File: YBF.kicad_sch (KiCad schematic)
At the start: 17 parts, among them J1 Chain_LED_out, J2 Chain_LED_return, SW1 1825910-6, SW2 1825910-6

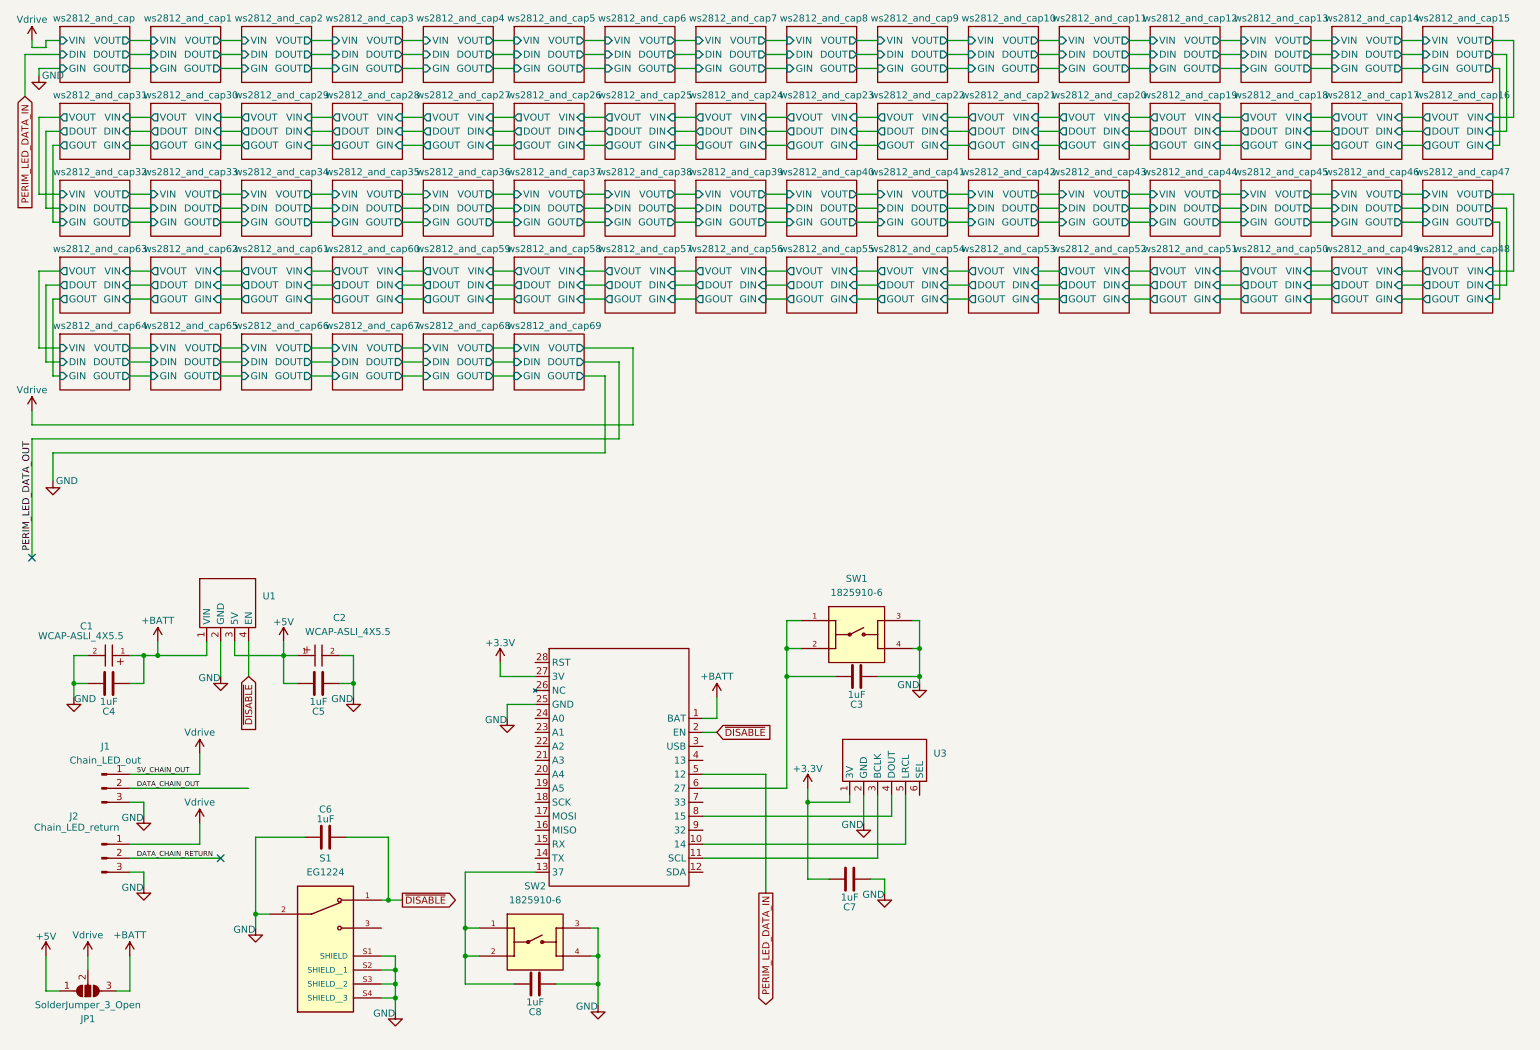
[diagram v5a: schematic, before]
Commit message: Add chain loop holes
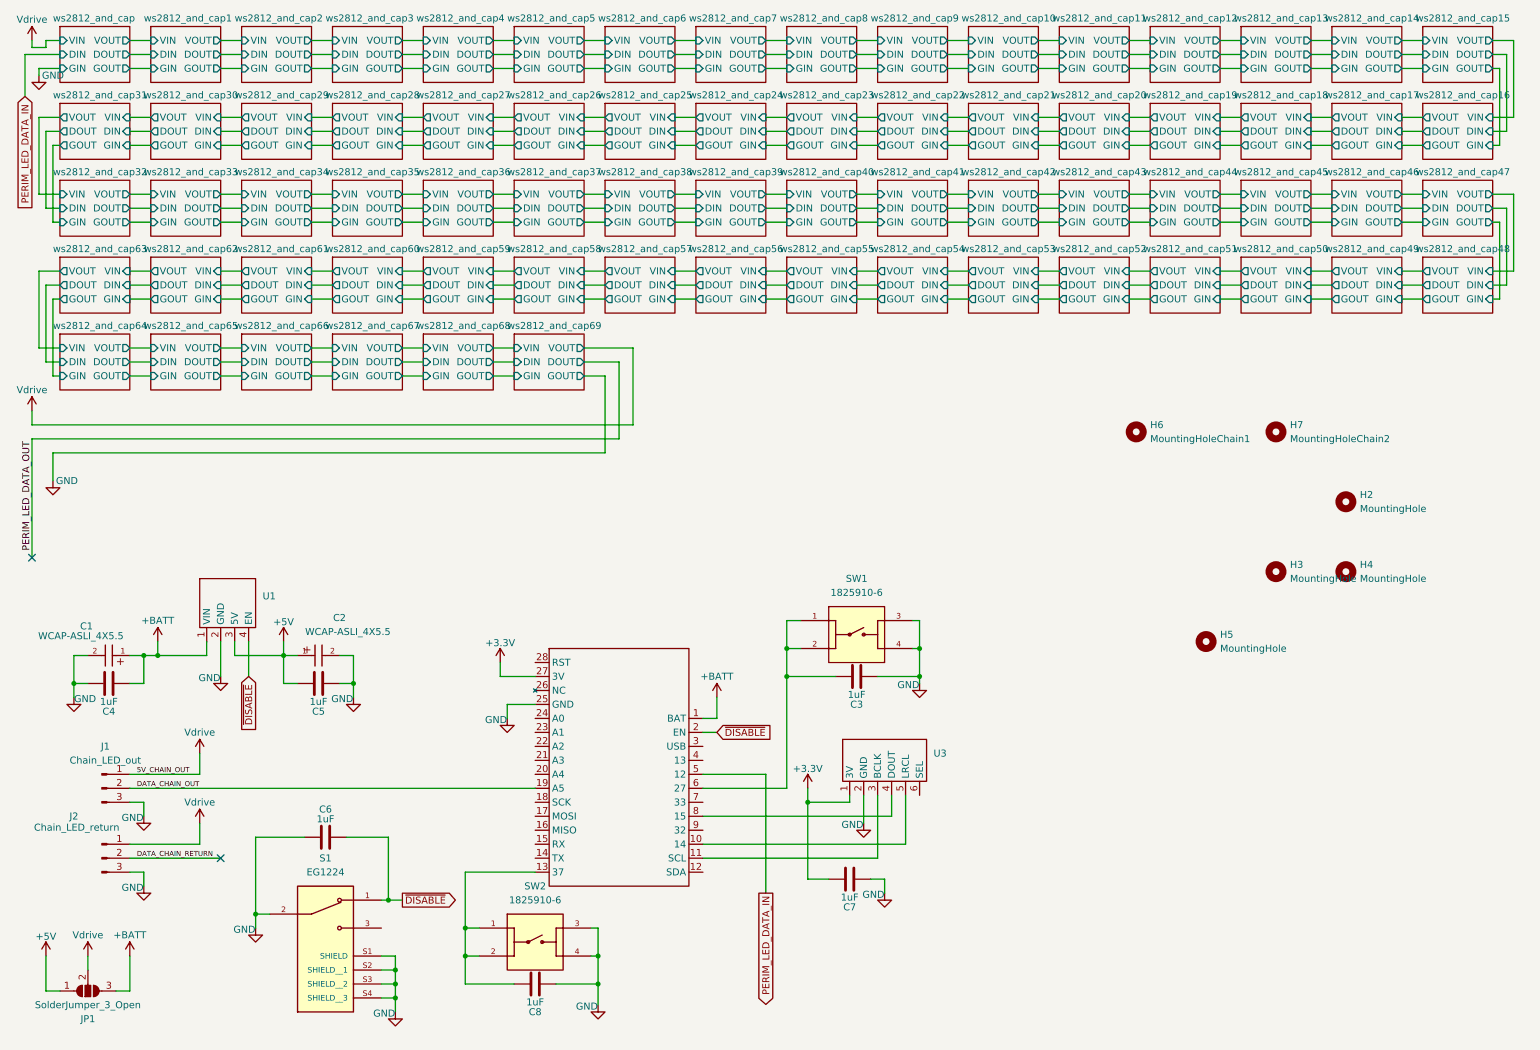
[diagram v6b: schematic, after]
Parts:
- added H2, H3, H4: MountingHole, MountingHole:MountingHole_3mm, symbol Mechanical:MountingHole
- added H5: MountingHole, MountingHole:MountingHole_6mm, symbol Mechanical:MountingHole
- added H6: MountingHoleChain1, MountingHole:MountingHole_2.1mm, symbol Mechanical:MountingHole
- added H7: MountingHoleChain2, MountingHole:MountingHole_2.1mm, symbol Mechanical:MountingHole
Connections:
- net DATA_CHAIN_OUT: now also U2.19 (A5)

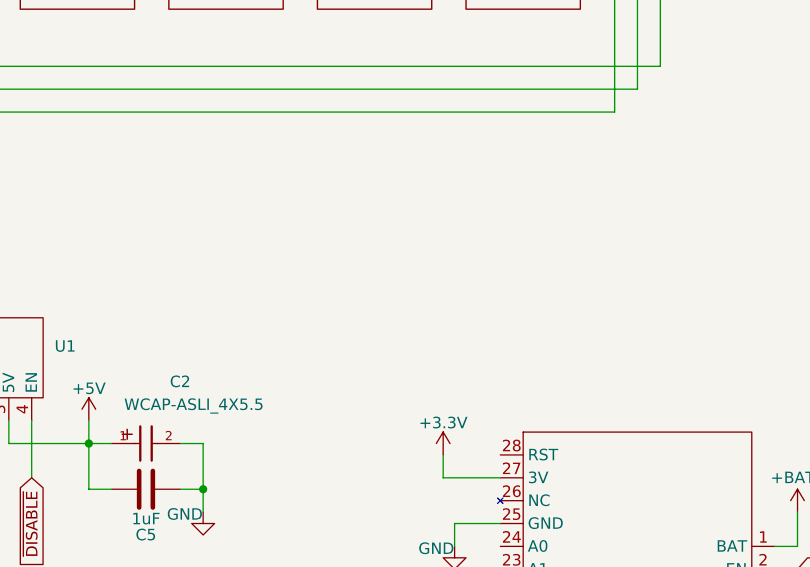
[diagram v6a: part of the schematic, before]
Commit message: add preliminary power saving FETS
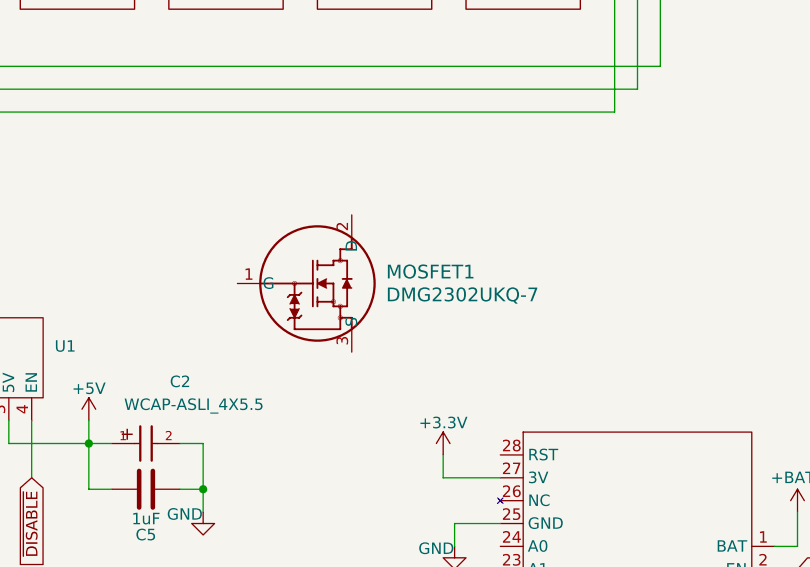
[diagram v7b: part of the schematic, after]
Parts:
- added MOSFET1: DMG2302UKQ-7, SOT23_DMG2302_DIO, symbol pfornage-kicad-lib:DMG2302UKQ-7
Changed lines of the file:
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@@
+	)
+	(symbol
+		(lib_id "pfornage-kicad-lib:DMG2302UKQ-7")
+		(at 77.47 111.76 0)
+		(unit 1)
+		(exclude_from_sim no)
+		(in_bom yes)
+		(on_board yes)
+		(dnp no)
+		(fields_autoplaced yes)
+		(property "Reference" "MOSFET1"
+			(at 93.98 110.4899 0)
+			(effects
+				(font
+					(size 1.524 1.524)
+				)
+				(justify left)
+			)
+		)
+		(property "Value" "DMG2302UKQ-7"
+			(at 93.98 113.0299 0)
+			(effects
+				(font
+					(size 1.524 1.524)
+				)
+				(justify left)
+			)
+		)
+		(property "Footprint" "SOT23_DMG2302_DIO"
+			(at 77.47 111.76 0)
+			(effects
+				(font
+					(size 1.27 1.27)
+					(italic yes)
+				)
+				(hide yes)
+			)
+		)
+		(property "Datasheet" "DMG2302UKQ-7"
+			(at 77.47 111.76 0)
+			(effects
+				(font
+					(size 1.27 1.27)
+					(italic yes)
+				)
+				(hide yes)
+			)
+		)
+		(property "Description" ""
+			(at 77.47 111.76 0)
+			(effects
+				(font
+					(size 1.27 1.27)
+				)
+				(hide yes)
+			)
+		)
+		(pin "3"
+		)
+		(pin "2"
+		)
+		(pin "1"
+		)
+		(instances
+			(project ""
+				(path "/05f069bc-566f-4102-818d-6b00a30fef11"
+					(reference "MOSFET1")
+					(unit 1)
+				)
+			)
+		)
 	)
 	(symbol

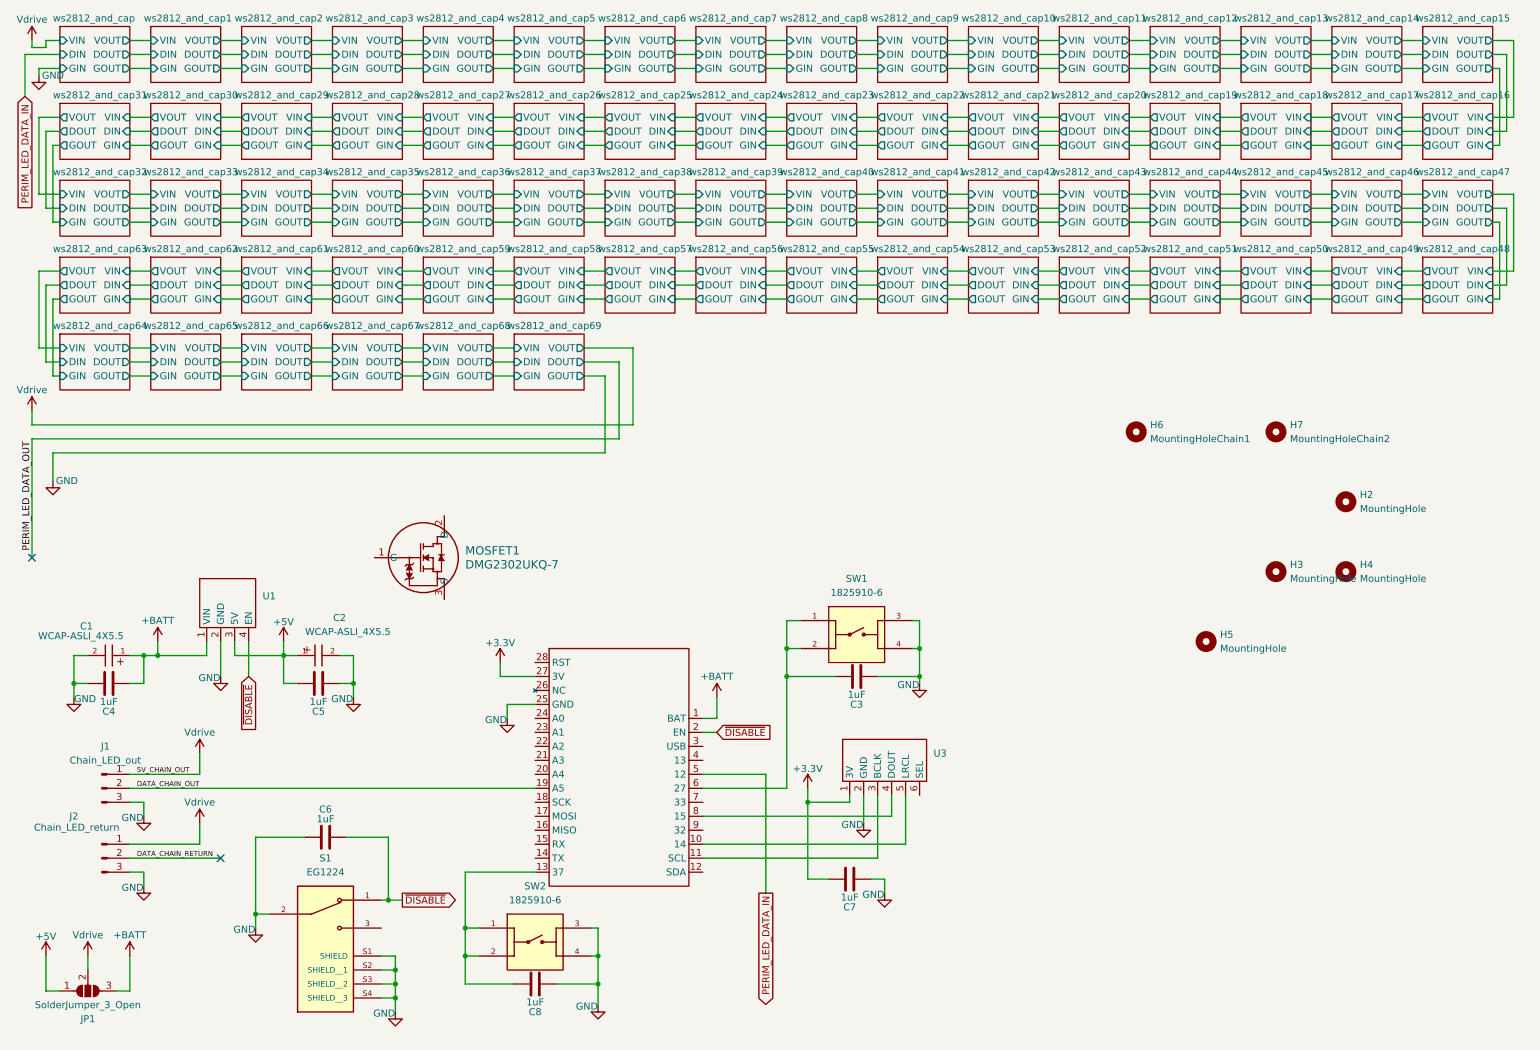
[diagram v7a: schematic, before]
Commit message: supporting FET impl
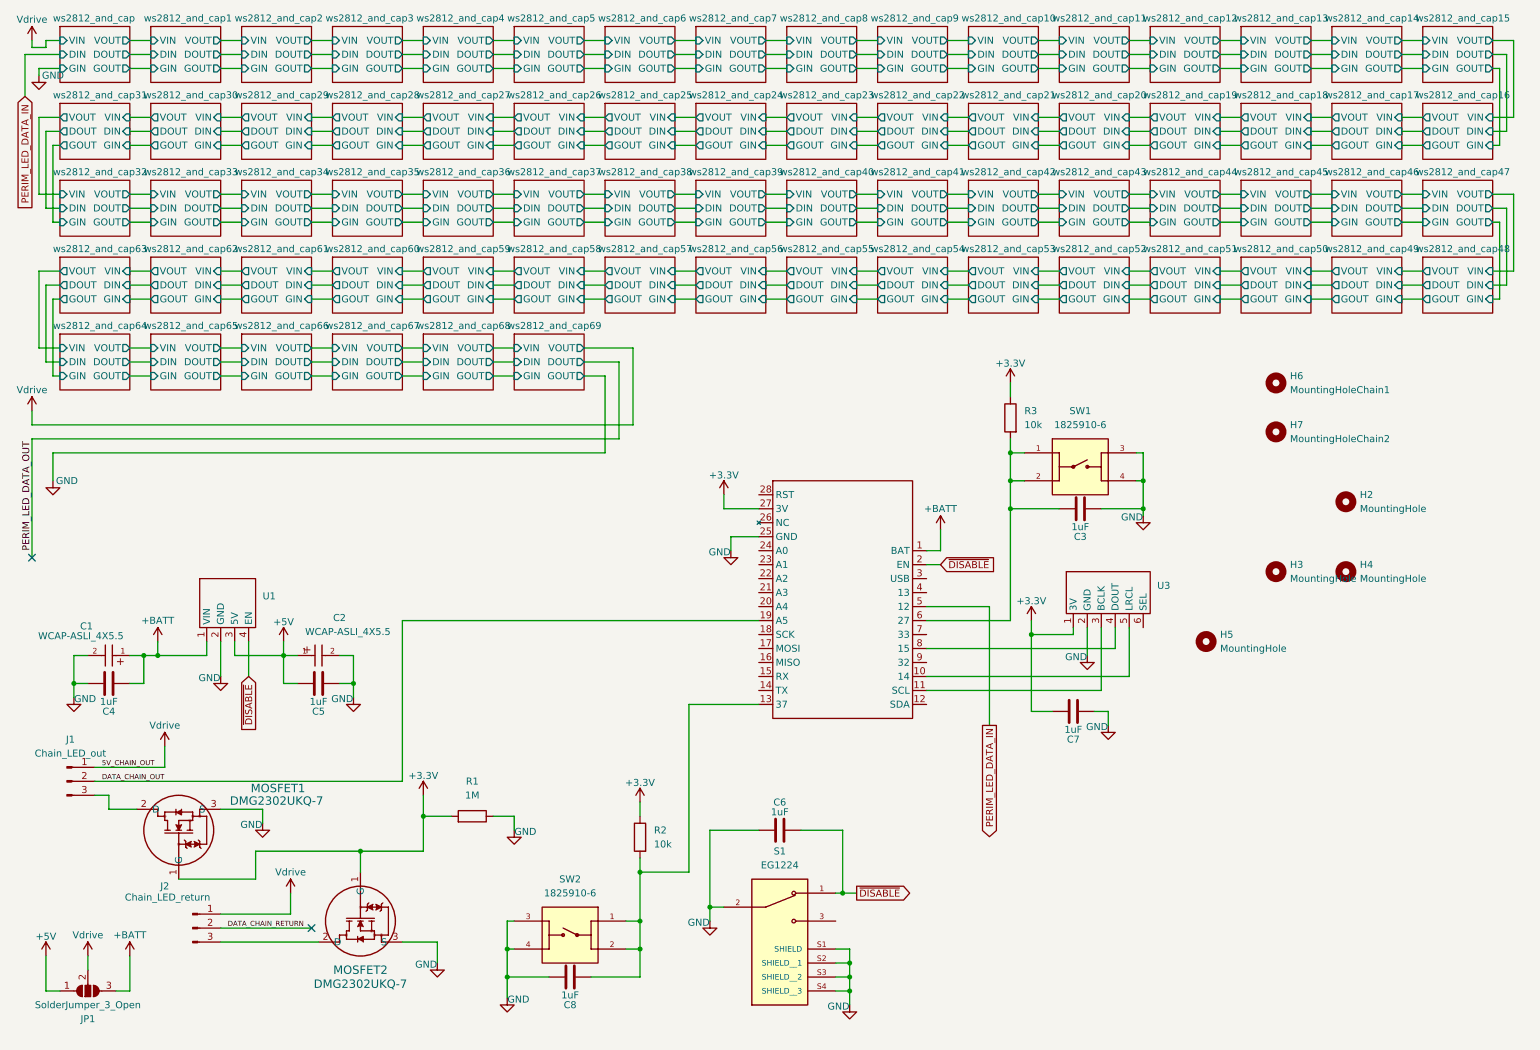
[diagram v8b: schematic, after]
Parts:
- added MOSFET2: DMG2302UKQ-7, SOT23_DMG2302_DIO, symbol pfornage-kicad-lib:DMG2302UKQ-7
- added R1: 1M, Resistor_SMD:R_0603_1608Metric, symbol Device:R
- added R2, R3: 10k, Resistor_SMD:R_0603_1608Metric, symbol Device:R
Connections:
- net +3.3V: now also MOSFET1.1 (G), MOSFET2.1 (G), R1.2, R2.1, R3.1
- net GND: now also MOSFET1.3 (S), MOSFET2.3 (S), R1.1; no longer J1.3 (Pin_3), J2.3 (Pin_3)
- net at C8.1, SW2.1, SW2.2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: now also R2.2
- net at C3.1, SW1.1, SW1.2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: now also R3.2
- net at MOSFET1.2 (D): now also J1.3 (Pin_3)
- new net: J2.3 (Pin_3), MOSFET2.2 (D)
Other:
- moved on the sheet: C3, C6, C7, C8, H6, J1, J2, MOSFET1, S1, SW1, SW2, U3
